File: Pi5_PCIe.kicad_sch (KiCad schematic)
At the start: 27 parts, among them IC1 MP2338GTL-P, J1 10018783-11200TLF, J2 12V IN, J3 Pi5 PCIe

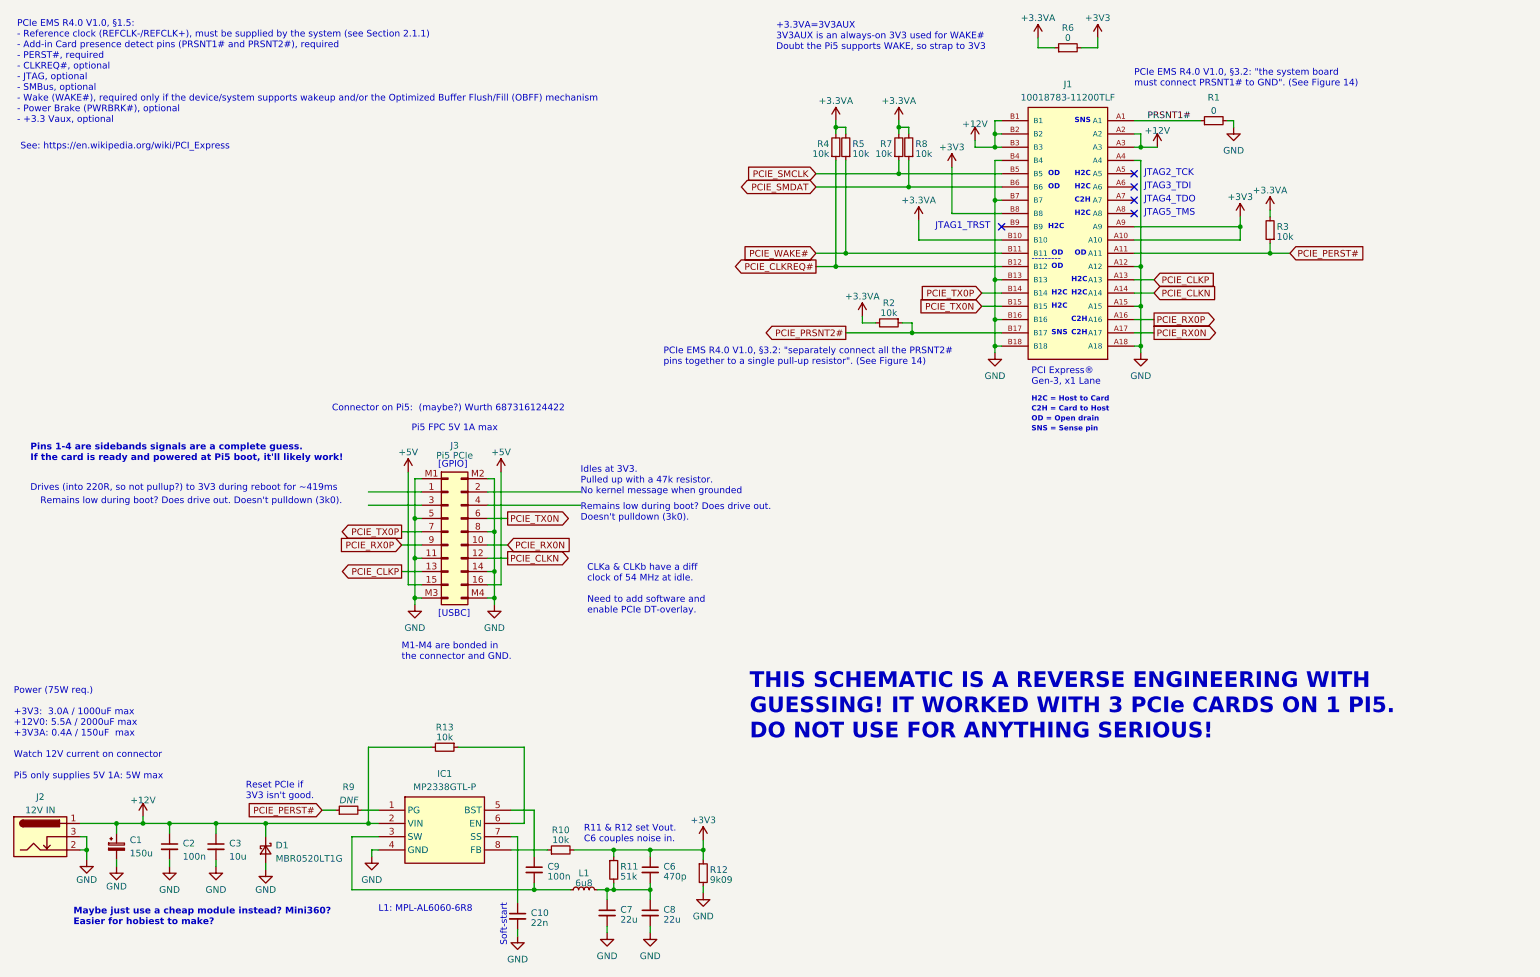
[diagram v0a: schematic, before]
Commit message: Schematic tweaks towards making a test PCB
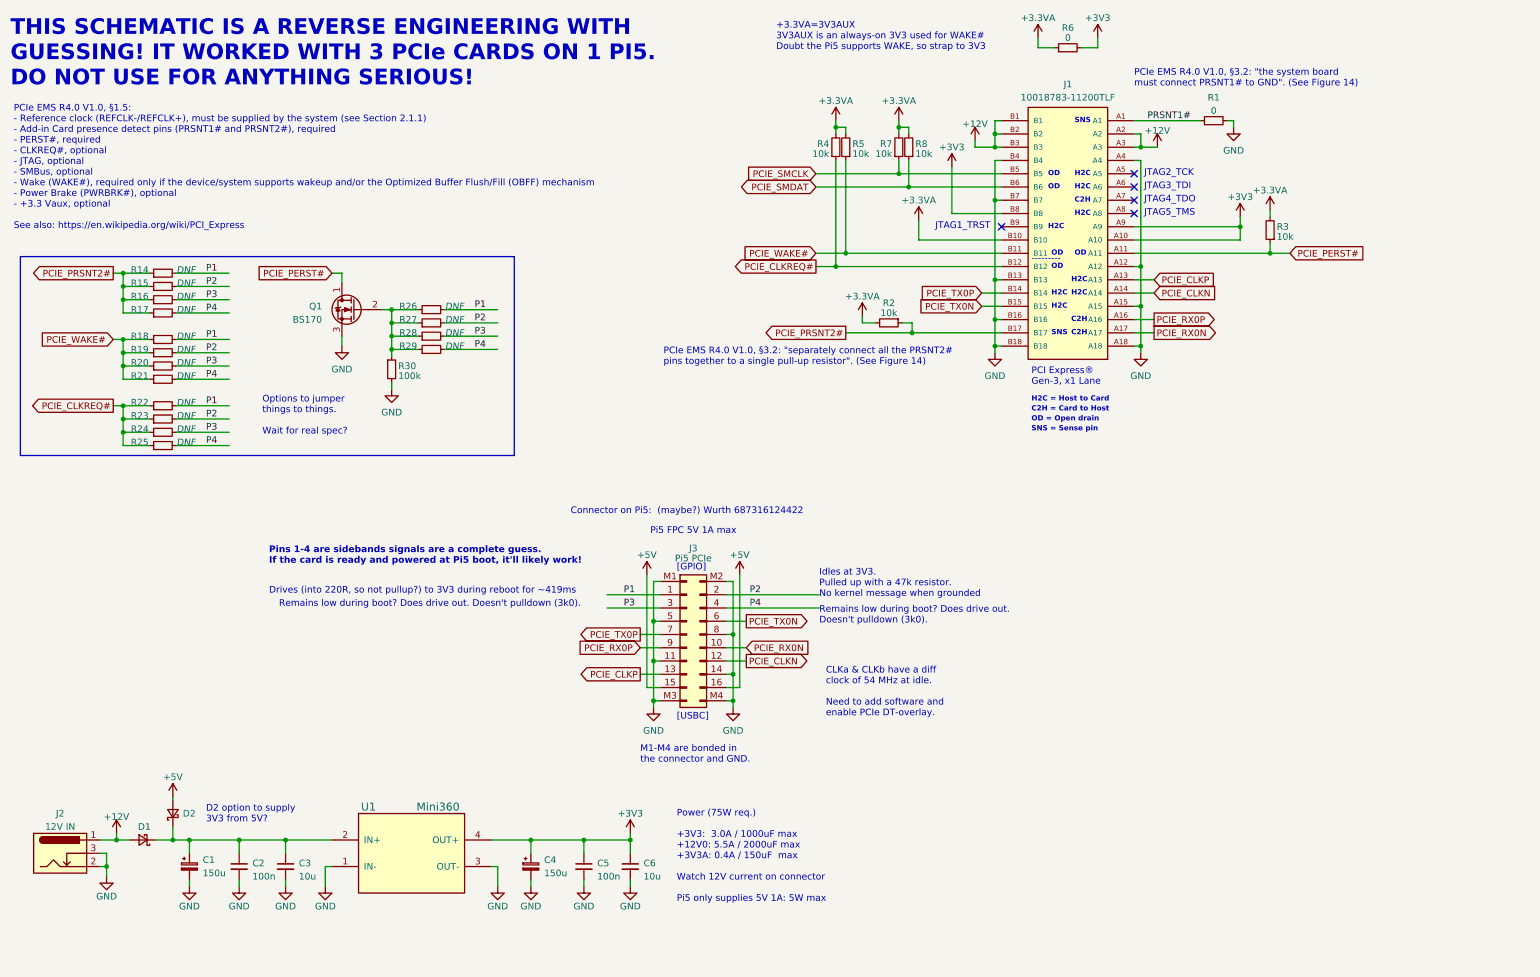
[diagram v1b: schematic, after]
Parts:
- removed C10: 22n, Capacitor_SMD:C_0603_1608Metric_Pad1.08x0.95mm_HandSolder, symbol Device:C_Small
- removed C7, C8: 22u, Capacitor_SMD:C_0603_1608Metric_Pad1.08x0.95mm_HandSolder, symbol Device:C_Small
- removed C9: 100n, Capacitor_SMD:C_0603_1608Metric_Pad1.08x0.95mm_HandSolder, symbol Device:C_Small
- removed IC1: MP2338GTL-P, SOTFL50P160X60-8N, symbol MP2338GTL-P:MP2338GTL-P
- removed L1: 6u8, symbol Device:L_Small
- removed R10, R13: 10k, symbol Device:R_Small
- removed R11: 51k, symbol Device:R_Small
- removed R12: 9k09, symbol Device:R_Small
- removed R9: DNF, symbol Device:R_Small
- added C4: 150u, Capacitor_SMD:CP_Elec_6.3x7.7, symbol Device:C_Polarized_Small
- added C5: 100n, Capacitor_SMD:C_0805_2012Metric_Pad1.18x1.45mm_HandSolder, symbol Device:C_Small
- added D2: MBR0520LT1G, Diode_SMD:D_SOD-123F, symbol Device:D_Schottky_Small
- added Q1: BS170, Package_TO_SOT_THT:TO-92_Inline, symbol Transistor_FET:BS170
- added R14, R15, R16, R17, R18, R19, R20, R21, R22, R23, R24, R25, R26, R27, R28, R29: DNF, symbol Device:R_Small
- added R30: 100k, symbol Device:R_Small
- added U1: Mini360, symbol Mini360:Mini360
- C2, C3: footprint Capacitor_SMD:C_0603_1608Metric_Pad1.08x0.95mm_HandSolder -> Capacitor_SMD:C_0805_2012Metric_Pad1.18x1.45mm_HandSolder
- C6: value 470p -> 10u; footprint Capacitor_SMD:C_0603_1608Metric_Pad1.08x0.95mm_HandSolder -> Capacitor_SMD:C_0805_2012Metric_Pad1.18x1.45mm_HandSolder
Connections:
- net +12V: now also D1.2 (A); no longer C1.1, C2.1, C3.1, D1.1 (K)
- net +3V3: now also C4.1, C5.1, U1.4 (OUT+)
- net +5V: now also D2.2 (A)
- net GND: now also C6.2, C4.2, C5.2, Q1.3 (S), R30.2, U1.1 (IN-), U1.3 (OUT-); no longer D1.2 (A)
- net PCIE_CLKREQ#: now also R22.1, R23.1, R24.1, R25.1
- net PCIE_PERST#: now also Q1.1 (D)
- net PCIE_PRSNT2#: now also R14.1, R15.1, R16.1, R17.1
- net PCIE_WAKE#: now also R18.1, R19.1, R20.1, R21.1
- net P1: now reaches J3.1 (Pin_3)
- net P1: now also R14.2, R18.2, R22.2, R26.2
- net P2: now reaches J3.2 (Pin_4)
- net P2: now also R15.2, R19.2, R23.2, R27.2
- net P3: now reaches J3.3 (Pin_5)
- net P3: now also R16.2, R20.2, R24.2, R28.2
- net P4: now reaches J3.4 (Pin_6)
- net P4: now also R17.2, R21.2, R25.2, R29.2
- new net: C1.1, C2.1, C3.1, D1.1 (K), D2.1 (K), U1.2 (IN+)
- new net: Q1.2 (G), R26.1, R27.1, R28.1, R29.1, R30.1
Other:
- note added: "D2 option to supply 3V3 from 5V?"
- note added: "Options to jumper things to things. Wait for real spec?"
- note removed: "L1: MPL-AL6060-6R8"
- note removed: "Maybe just use a cheap module instead? Mini360? Easier for hobiest to make?"
- note removed: "R11 & R12 set Vout. C6 couples noise in."
- note removed: "Reset PCIe if 3V3 isn't good."
- note removed: "See: https://en.wikipedia.org/wiki/PCI_Express"
- note removed: "Soft-start"
- moved on the sheet: C1, C2, C3, J2, J3

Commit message: Updated schematic based on testing & PCB layout * Used pinctrl to find out what P3 & P4 did, as suggested by @trejan * Reviewed Pi5 layout under connector to see that I had RX(P|N) swapped
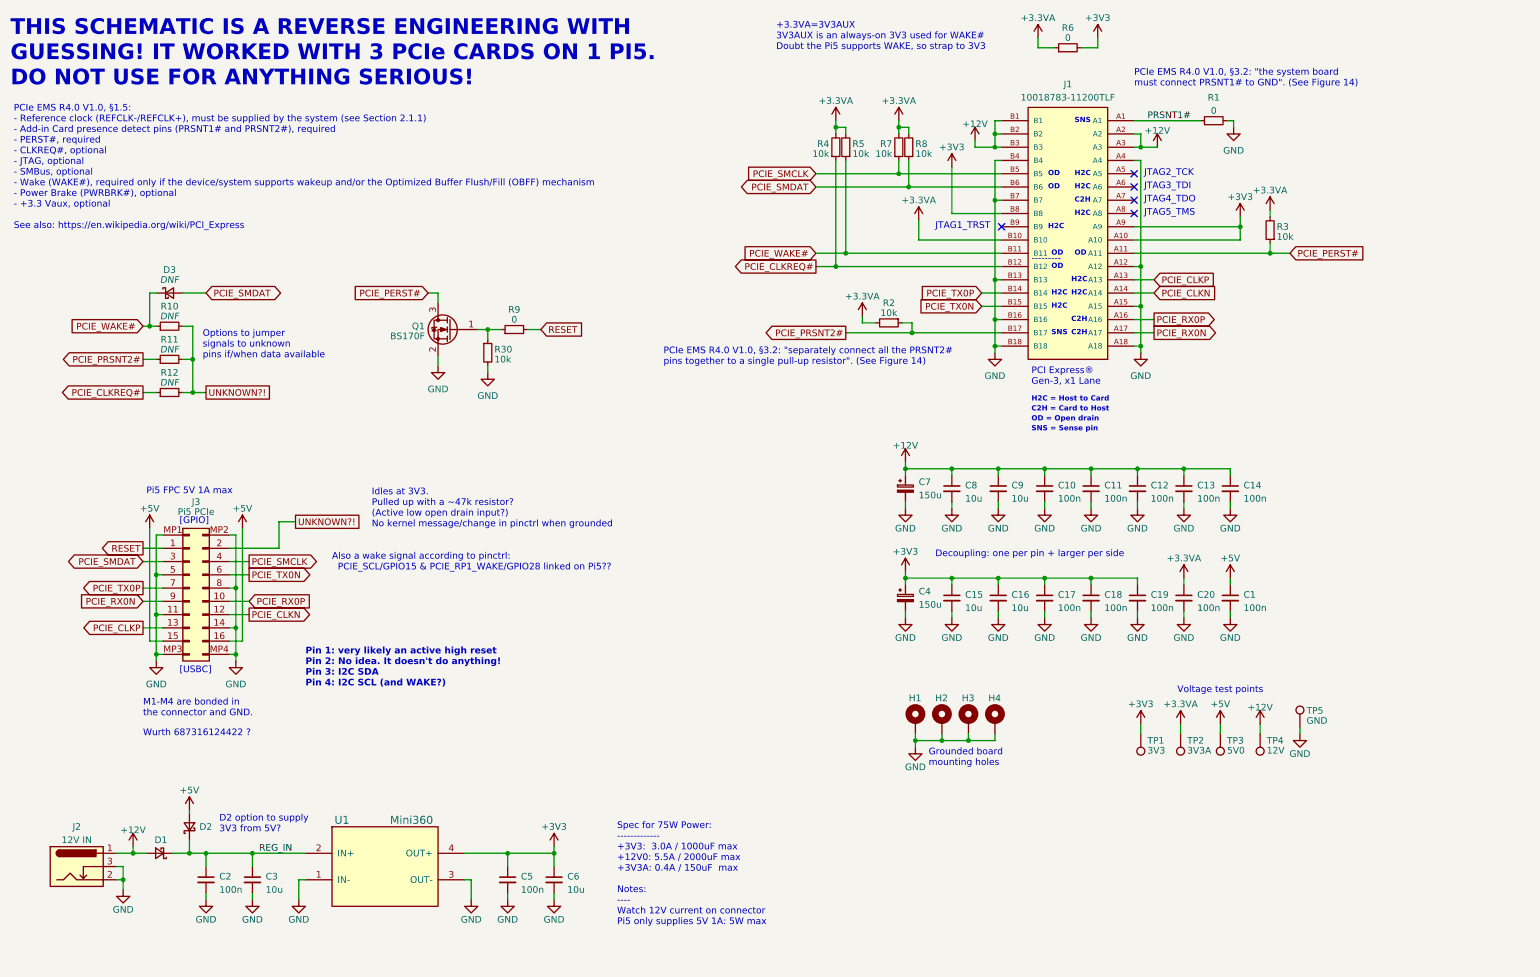
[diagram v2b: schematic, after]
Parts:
- removed C1: 150u, Capacitor_SMD:CP_Elec_6.3x7.7, symbol Device:C_Polarized_Small
- removed Q1: BS170, Package_TO_SOT_THT:TO-92_Inline, symbol Transistor_FET:BS170
- removed R14, R15, R16, R17, R18, R19, R20, R21, R22, R23, R24, R25, R26, R27, R28, R29: DNF, symbol Device:R_Small
- added C1, C10, C11, C12, C13, C14, C17, C18, C19, C20: 100n, Capacitor_SMD:C_0805_2012Metric_Pad1.18x1.45mm_HandSolder, symbol Device:C_Small
- added C15, C16, C8, C9: 10u, Capacitor_SMD:C_0805_2012Metric_Pad1.18x1.45mm_HandSolder, symbol Device:C_Small
- added C7: 150u, Capacitor_SMD:CP_Elec_6.3x7.7, symbol Device:C_Polarized_Small
- added D3: DNF, Diode_SMD:D_SOD-123F, symbol Device:D_Schottky_Small
- added H1, H2, H3, H4: MountingHole_Pad, MountingHole:MountingHole_3.2mm_M3_Pad_Via, symbol Mechanical:MountingHole_Pad
- added Q1: BS170F, Package_TO_SOT_SMD:SOT-23, symbol Transistor_FET:BS170F
- added R10, R11, R12: DNF, Capacitor_SMD:C_0805_2012Metric_Pad1.18x1.45mm_HandSolder, symbol Device:R_Small
- added R9: 0, Capacitor_SMD:C_0805_2012Metric_Pad1.18x1.45mm_HandSolder, symbol Device:R_Small
- added TP1: 3V3, TestPoint:TestPoint_Pad_D1.5mm, symbol Connector:TestPoint
- added TP2: 3V3A, TestPoint:TestPoint_Pad_D1.5mm, symbol Connector:TestPoint
- added TP3: 5V0, TestPoint:TestPoint_Pad_D1.5mm, symbol Connector:TestPoint
- added TP4: 12V, TestPoint:TestPoint_Pad_D1.5mm, symbol Connector:TestPoint
- added TP5: GND, TestPoint:TestPoint_Pad_D1.5mm, symbol Connector:TestPoint
- D1: value MBR0520LT1G -> (12V)
- D2: value MBR0520LT1G -> (5V)
- J3: footprint (none) -> FPC_conn:687316124422
- R1, R2, R3, R4, R5, R6, R7, R8: footprint (none) -> Capacitor_SMD:C_0805_2012Metric_Pad1.18x1.45mm_HandSolder
- R30: value 100k -> 10k; footprint (none) -> Capacitor_SMD:C_0805_2012Metric_Pad1.18x1.45mm_HandSolder
- U1: footprint (none) -> Mini360:Mini360_step-down
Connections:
- net P3 is gone; now on net PCIE_SMDAT: J3.3 (Pin_5)
- net P4 is gone; now on net PCIE_SMCLK: J3.4 (Pin_6)
- net +12V: now also C10.1, C11.1, C12.1, C13.1, C14.1, C7.1, C8.1, C9.1, TP4.1
- net +3.3VA: now also C20.1, TP2.1
- net +3V3: now also C15.1, C16.1, C17.1, C18.1, C19.1, TP1.1
- net +5V: now also C1.1, TP3.1
- net GND: now also J3.MP1, J3.MP2, J3.MP3, J3.MP4, C1.2, C10.2, C11.2, C12.2, C13.2, C14.2, C15.2, C16.2, C17.2, C18.2, C19.2, C20.2, C7.2, C8.2, C9.2, H1.1, H2.1, H3.1, H4.1, Q1.2 (S), TP5.1; no longer J3.M1 (Pin_1), J3.M2 (Pin_2), J3.M3 (Pin_19), J3.M4 (Pin_20)
- net PCIE_CLKREQ#: now also R12.1
- net PCIE_PERST#: now also Q1.3 (D)
- net PCIE_PRSNT2#: now also R11.1
- net PCIE_RX0N: now also J3.9 (Pin_11); no longer J3.10 (Pin_12)
- net PCIE_RX0P: now also J3.10 (Pin_12); no longer J3.9 (Pin_11)
- net PCIE_SMDAT: now also D3.2 (A)
- net PCIE_WAKE#: now also D3.1 (K), R10.1
- net REG_IN: now reaches C2.1, C3.1, D1.1 (K), D2.1 (K), U1.2 (IN+)
- net at R30.1: now also Q1.1 (G), R9.1
- net P1 renamed RESET
- net RESET: now also R9.2
- net P2 renamed UNKNOWN?!
- net UNKNOWN?!: now also R10.2, R11.2, R12.2
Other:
- note added: "Also a wake signal according to pinctrl: PCIE_SCL/GPIO15 & PCIE_RP1_WAKE/GPIO28 linked on Pi5??"
- note added: "Decoupling: one per pin + larger per side"
- note added: "Grounded board mounting holes"
- note added: "Idles at 3V3. Pulled up with a ~47k resistor? (Active low open drain input?) No kernel message/change in pinctrl when grounded"
- note added: "Options to jumper signals to unknown pins if/when data available"
- note added: "Pin 1: very likely an active high reset Pin 2: No idea. It doesn't do anything! Pin 3: I2C SDA Pin 4: I2C SCL (and WAKE?)"
- note added: "Spec for 75W Power: ------------- +3V3: 3.0A / 1000uF max +12V0: 5.5A / 2000uF max +3V3A: 0.4A / 150uF max Notes: ---- Watch 12V current on connector Pi5 only supplies 5V 1A: 5W max"
- note added: "Voltage test points"
- note added: "Wurth 687316124422 ?"
- note removed: "CLKa & CLKb have a diff clock of 54 MHz at idle. Need to add software and enable PCIe DT-overlay."
- note removed: "Connector on Pi5: (maybe?) Wurth 687316124422"
- note removed: "Drives (into 220R, so not pullup?) to 3V3 during reboot for ~419ms"
- note removed: "Idles at 3V3. Pulled up with a 47k resistor. No kernel message when grounded"
- note removed: "Options to jumper things to things. Wait for real spec?"
- note removed: "Pins 1-4 are sidebands signals are a complete guess. If the card is ready and powered at Pi5 boot, it'll likely work!"
- note removed: "Power (75W req.) +3V3: 3.0A / 1000uF max +12V0: 5.5A / 2000uF max +3V3A: 0.4A / 150uF max Watch 12V current on connector Pi5 only supplies 5V 1A: 5W max"
- note removed: "Remains low during boot? Does drive out. Doesn't pulldown (3k0)."
- moved on the sheet: C2, C3, C5, C6, D1, D2, J2, J3, R30, U1

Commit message: Quick test PCIe breakout board
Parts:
- added D4: PWR, LED_SMD:LED_0805_2012Metric_Pad1.15x1.40mm_HandSolder, symbol Device:LED
- added D5: RST, LED_SMD:LED_0805_2012Metric_Pad1.15x1.40mm_HandSolder, symbol Device:LED
- added R14, R15: 1k, Resistor_SMD:R_0805_2012Metric_Pad1.20x1.40mm_HandSolder, symbol Device:R_Small
- D2: renamed from D3; footprint Diode_SMD:D_SOD-123F -> Diode_SMD:D_0805_2012Metric_Pad1.15x1.40mm_HandSolder
- R1: renamed from R10; footprint Capacitor_SMD:C_0805_2012Metric_Pad1.18x1.45mm_HandSolder -> Resistor_SMD:R_0805_2012Metric_Pad1.20x1.40mm_HandSolder
- R10: renamed from R8; footprint Capacitor_SMD:C_0805_2012Metric_Pad1.18x1.45mm_HandSolder -> Resistor_SMD:R_0805_2012Metric_Pad1.20x1.40mm_HandSolder
- R11: renamed from R6; footprint Capacitor_SMD:C_0805_2012Metric_Pad1.18x1.45mm_HandSolder -> Resistor_SMD:R_0805_2012Metric_Pad1.20x1.40mm_HandSolder
- R12: renamed from R1; footprint Capacitor_SMD:C_0805_2012Metric_Pad1.18x1.45mm_HandSolder -> Resistor_SMD:R_0805_2012Metric_Pad1.20x1.40mm_HandSolder
- R13: renamed from R3; footprint Capacitor_SMD:C_0805_2012Metric_Pad1.18x1.45mm_HandSolder -> Resistor_SMD:R_0805_2012Metric_Pad1.20x1.40mm_HandSolder
- R2: renamed from R11; footprint Capacitor_SMD:C_0805_2012Metric_Pad1.18x1.45mm_HandSolder -> Resistor_SMD:R_0805_2012Metric_Pad1.20x1.40mm_HandSolder
- R3: renamed from R12; footprint Capacitor_SMD:C_0805_2012Metric_Pad1.18x1.45mm_HandSolder -> Resistor_SMD:R_0805_2012Metric_Pad1.20x1.40mm_HandSolder
- R4: renamed from R30; footprint Capacitor_SMD:C_0805_2012Metric_Pad1.18x1.45mm_HandSolder -> Resistor_SMD:R_0805_2012Metric_Pad1.20x1.40mm_HandSolder
- R5: renamed from R9; footprint Capacitor_SMD:C_0805_2012Metric_Pad1.18x1.45mm_HandSolder -> Resistor_SMD:R_0805_2012Metric_Pad1.20x1.40mm_HandSolder
- R6: renamed from R4; footprint Capacitor_SMD:C_0805_2012Metric_Pad1.18x1.45mm_HandSolder -> Resistor_SMD:R_0805_2012Metric_Pad1.20x1.40mm_HandSolder
- R7: renamed from R5; footprint Capacitor_SMD:C_0805_2012Metric_Pad1.18x1.45mm_HandSolder -> Resistor_SMD:R_0805_2012Metric_Pad1.20x1.40mm_HandSolder
- R8: renamed from R2; footprint Capacitor_SMD:C_0805_2012Metric_Pad1.18x1.45mm_HandSolder -> Resistor_SMD:R_0805_2012Metric_Pad1.20x1.40mm_HandSolder
- R9: renamed from R7; footprint Capacitor_SMD:C_0805_2012Metric_Pad1.18x1.45mm_HandSolder -> Resistor_SMD:R_0805_2012Metric_Pad1.20x1.40mm_HandSolder
- renumbered C2 to C1, C16 to C10, C10 to C11, C17 to C12, C11 to C13, C18 to C14, C12 to C15, C19 to C16, C13 to C17, C20 to C18, C14 to C19, C3 to C2, C1 to C20, C5 to C3, C6 to C4, C7 to C5, C4 to C6, C8 to C7, C15 to C8, D2 to D3, J2 to J1, J3 to J2, J1 to J3
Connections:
- net +3V3: now also R14.1
- net GND: now also D4.1 (K), D5.1 (K)
- net RESET: now also R15.1
- new net: D4.2 (A), R14.2
- new net: D5.2 (A), R15.2
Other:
- note added: "D3 option to supply 3V3 from 5V?"
- note added: "GRN"
- note added: "RED"
- note removed: "D2 option to supply 3V3 from 5V?"
